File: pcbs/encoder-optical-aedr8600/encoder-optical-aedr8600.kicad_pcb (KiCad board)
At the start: 2 copper layers, 10 x 6 mm, 10 parts, among them J101 BM05B-GHS, U101 AEDR-8600-100

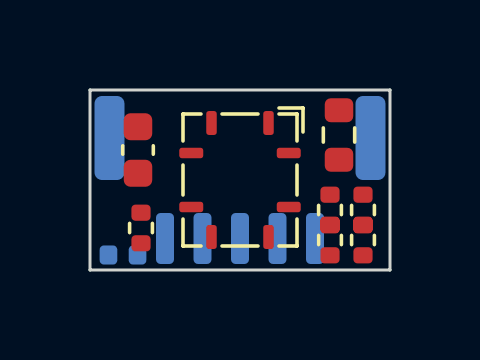
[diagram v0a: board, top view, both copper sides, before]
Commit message: Finish encoder-optical-aedr8600 PCB layout
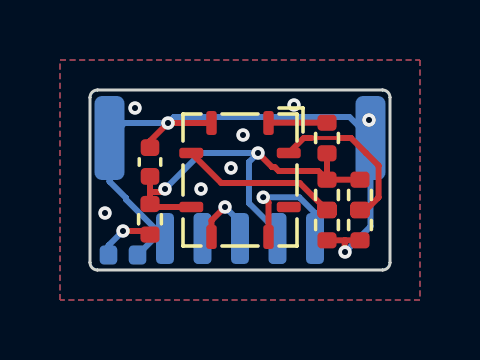
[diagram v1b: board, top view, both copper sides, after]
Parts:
- C101: footprint Capacitor_SMD:C_0603_1608Metric -> Capacitor_SMD:C_0402_1005Metric
- R101: footprint Resistor_SMD:R_0603_1608Metric -> Resistor_SMD:R_0402_1005Metric
- moved C101 0.57 mm to (147.0, 99.4)
- moved R102 0.51 mm to (154.0, 100.5)
- moved R103 0.51 mm to (154.0, 101.5)
- moved R104 0.51 mm to (152.9, 100.5)
- moved R105 0.51 mm to (152.9, 101.5)
- moved R106 0.42 mm to (147.0, 101.3)
- moved R101 0.41 mm to (152.9, 98.6)
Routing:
- net GND: track 0.00 -> 22.7 mm, vias 0 -> 9
- net +5V: track 0.00 -> 14.5 mm, vias 0 -> 2
- net /SEL_2X: track 0.00 -> 5.45 mm
- net /SEL_4X: track 0.00 -> 5.32 mm
- net Net-(J101-Pad1): track 0.00 -> 4.19 mm, vias 0 -> 1
- net Net-(J101-Pad3): track 0.00 -> 2.44 mm, vias 0 -> 1
- net Net-(R101-Pad2): track 0.00 -> 1.95 mm
- net Net-(D101-Pad2): track 0.00 -> 1.95 mm, vias 0 -> 1
- added copper zone on B.Cu, net GND
- added copper zone on F.Cu, net GND
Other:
- outline, holes or cut-outs redrawn

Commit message: Increase outline corner radius
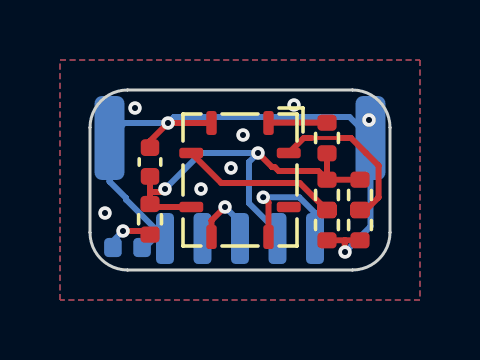
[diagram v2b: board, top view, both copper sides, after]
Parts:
- moved D101 0.29 mm to (146.2, 102.2)
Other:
- outline, holes or cut-outs redrawn
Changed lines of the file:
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@@
   )
   (footprint "LED_SMD:LED_0402_1005Metric" (layer "B.Cu")
-    (at 146.1 102.5 180)
+    (at 146.25 102.25 180)
     (descr "LED SMD 0402 (1005 Metric), square (rectangular) end terminal, IPC_7351 nominal, (Body size source: http://www.tortai-tech.com/upload/download/2011102023233369053.pdf), generated with kicad-footprint-generator")
     (tags "LED")
@@
     )
   )
-  (gr_line (start 154.75 103) (end 145.25 103) (layer "Edge.Cuts") (width 0.1))
-  (gr_arc (start 155 102.75) (mid 154.926777 102.926777) (end 154.75 103) (layer "Edge.Cuts") (width 0.1))
-  (gr_line (start 145 102.75) (end 145 97.25) (layer "Edge.Cuts") (width 0.1))
-  (gr_arc (start 154.75 97) (mid 154.926777 97.073223) (end 155 97.25) (layer "Edge.Cuts") (width 0.1))
-  (gr_arc (start 145 97.25) (mid 145.073223 97.073223) (end 145.25 97) (layer "Edge.Cuts") (width 0.1))
-  (gr_line (start 145.25 97) (end 154.75 97) (layer "Edge.Cuts") (width 0.1))
-  (gr_line (start 155 97.25) (end 155 102.75) (layer "Edge.Cuts") (width 0.1))
-  (gr_arc (start 145.25 103) (mid 145.073223 102.926777) (end 145 102.75) (layer "Edge.Cuts") (width 0.1))
+  (gr_line (start 153.75 103) (end 146.25 103) (layer "Edge.Cuts") (width 0.1))
+  (gr_line (start 145 101.75) (end 145 98.25) (layer "Edge.Cuts") (width 0.1))
+  (gr_arc (start 153.75 97) (mid 154.633883 97.366117) (end 155 98.25) (layer "Edge.Cuts") (width 0.1))
+  (gr_arc (start 155 101.75) (mid 154.633883 102.633883) (end 153.75 103) (layer "Edge.Cuts") (width 0.1))
+  (gr_arc (start 146.25 103) (mid 145.366117 102.633883) (end 145 101.75) (layer "Edge.Cuts") (width 0.1))
+  (gr_arc (start 145 98.25) (mid 145.366117 97.366117) (end 146.25 97) (layer "Edge.Cuts") (width 0.1))
+  (gr_line (start 146.25 97) (end 153.75 97) (layer "Edge.Cuts") (width 0.1))
+  (gr_line (start 155 98.25) (end 155 101.75) (layer "Edge.Cuts") (width 0.1))
   (dimension (type aligned) (layer "Dwgs.User")
     (pts (xy 145 102.75) (xy 155 102.75))
@@
   (segment (start 147.5 101.95) (end 147.135 101.95) (width 0.2) (layer "B.Cu") (net 2))
   (segment (start 153.65 97.9) (end 147.8 97.9) (width 0.2) (layer "B.Cu") (net 2))
-  (segment (start 147.135 101.95) (end 146.585 102.5) (width 0.2) (layer "B.Cu") (net 2))
+  (segment (start 146.735 102.25) (end 146.835 102.25) (width 0.2) (layer "B.Cu") (net 2))
   (segment (start 147.8 97.9) (end 147.6 98.1) (width 0.2) (layer "B.Cu") (net 2))
   (segment (start 145.65 100.05) (end 145.65 98.6) (width 0.2) (layer "B.Cu") (net 2))
   (segment (start 154.35 98.6) (end 153.65 97.9) (width 0.2) (layer "B.Cu") (net 2))
+  (segment (start 146.835 102.25) (end 147.135 101.95) (width 0.2) (layer "B.Cu") (net 2))
   (segment (start 146.2 100.6) (end 145.65 100.05) (width 0.2) (layer "B.Cu") (net 2))
   (segment (start 147.6 98.1) (end 146.15 98.1) (width 0.2) (layer "B.Cu") (net 2))
@@
   (segment (start 146.1 101.7) (end 146.88 101.7) (width 0.2) (layer "F.Cu") (net 3))
   (via (at 146.1 101.7) (size 0.45) (drill 0.2) (layers "F.Cu" "B.Cu") (net 3))
-  (segment (start 145.615 102.5) (end 145.615 102.185) (width 0.2) (layer "B.Cu") (net 3))
   (segment (start 145.615 102.185) (end 146.1 101.7) (width 0.2) (layer "B.Cu") (net 3))
   (segment (start 150.95 101.9) (end 150.95 100.750625) (width 0.2) (layer "F.Cu") (net 4))
